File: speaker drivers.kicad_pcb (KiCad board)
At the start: 2 copper layers, 62.9 x 54 mm, 32 parts, among them CN1 68uFE, CN2 10uFE, CN3 0.1uFC

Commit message: Speaker drivers V1 ready for fabrication
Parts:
- removed LOUT1, ROUT1: BNC, LBHB:BNC_Socket_TYCO-AMP_RevA_Date21Jun2010
- added OUT1: CONN_01X04, Socket_Strips:Socket_Strip_Straight_1x04, F.Cu at (88.8, 53.6)
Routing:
- net AGND: track 137.2 -> 118.5 mm
- net Net-(BUFR1-Pad4): track 19.2 -> 29.6 mm, vias 0 -> 1
- net Net-(BUFL1-Pad4): track 19.4 -> 27.0 mm, vias 0 -> 1
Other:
- board size 62.9 x 54 mm -> 54 x 54 mm
- board text added: "LGND"
- board text added: "LOUT"
- board text added: "RGND"
- board text added: "ROUT"

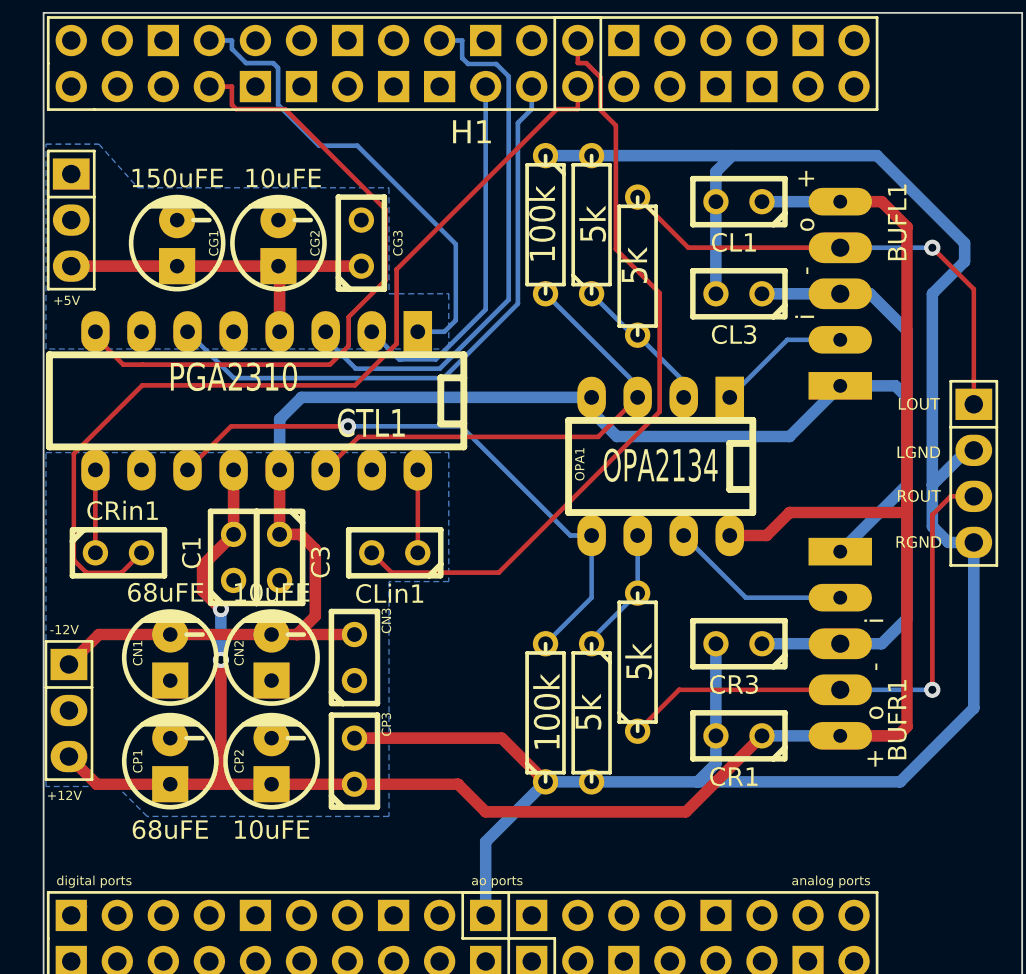
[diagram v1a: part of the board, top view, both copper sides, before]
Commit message: Fixes to speaker driver circuit
* Ensure bypass caps between -12V and GND are correct orientation
* Add notation for all caps indicating size
* Widen drill holes in BUF634
* Ensure cap symbols show orientation when needed
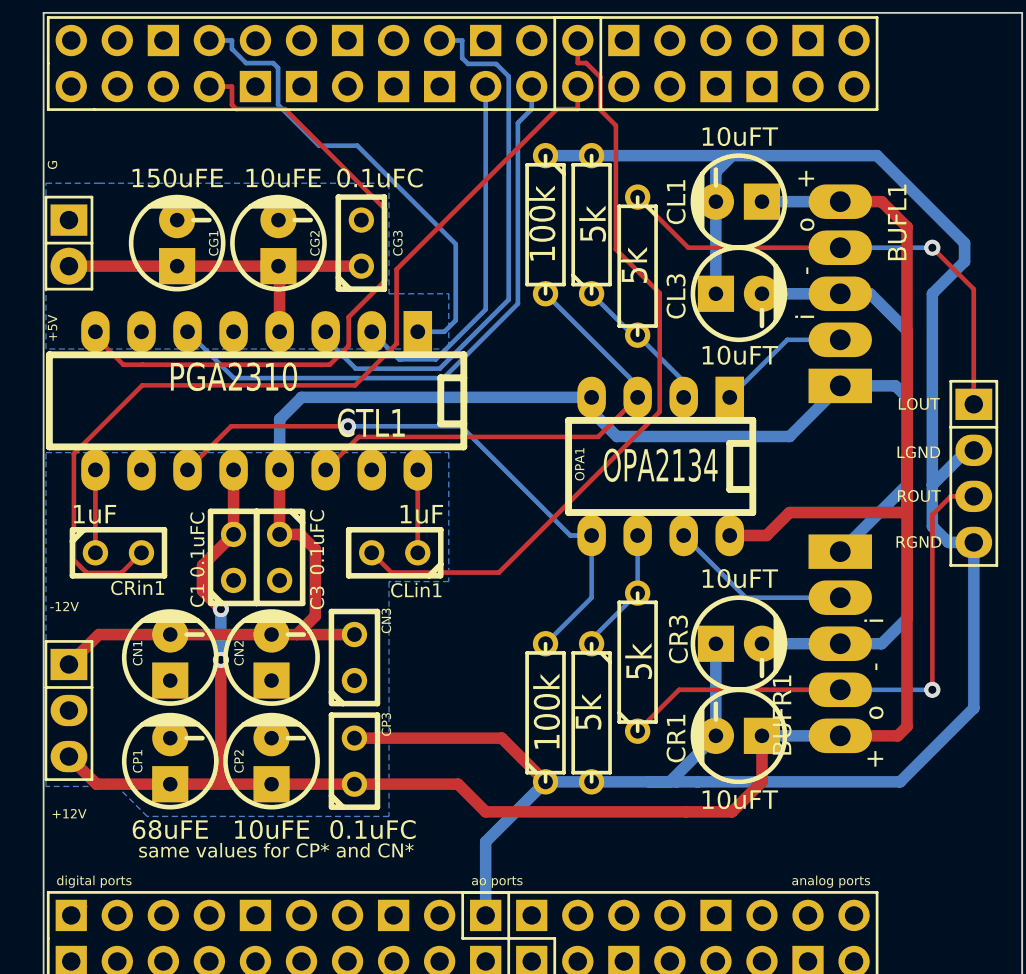
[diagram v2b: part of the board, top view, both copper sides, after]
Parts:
- CL1, CL3, CR1, CR3: footprint Discret:C1 -> Capacitors_ThroughHole:Capacitor5x6RM2.5
- DPWR1: value CONN_01X03 -> CONN_01X02; footprint Socket_Strips:Socket_Strip_Straight_1x03 -> Socket_Strips:Socket_Strip_Straight_1x02
- moved DPWR1 1.28 mm to (38.9, 40.9)
- turned CL1 to 90 degrees
- turned CL3 to 270 degrees
- turned CR1 to 90 degrees
- turned CR3 to 270 degrees
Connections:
- CL3 pad 1: -12V -> AGND
- CL3 pad 2: AGND -> -12V
- CR3 pad 1: -12V -> AGND
- CR3 pad 2: AGND -> -12V
- DPWR1 pad 1: Net-(DPWR1-Pad1) -> DGND
- DPWR1 pad 2: DGND -> +5V
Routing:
- net +12V: track 115.5 -> 117.0 mm
- net AGND: track 118.5 -> 119.9 mm
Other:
- board text added: "G"
- board text added: "same values for CP* and CN*"

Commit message: Commit before modifying speaker driver schematic
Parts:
- removed CG1: 150uFE, Capacitors_ThroughHole:Capacitor5x6RM2.5
- removed CN1, CP1: 68uFE, Capacitors_ThroughHole:Capacitor5x6RM2.5
- removed DPWR1: CONN_01X02, Socket_Strips:Socket_Strip_Straight_1x02
- removed H1: NI_header, LBHB:2x2x18
- removed OUT1: CONN_01X04, Socket_Strips:Socket_Strip_Straight_1x04
- added COMM1: CONN_01X05, Socket_Strips:Socket_Strip_Straight_1x05, F.Cu at (44.5, 36.1)
- added OUTL1: BNC, LBHB:BNC_Socket_TYCO-AMP_RevA_Date21Jun2010, F.Cu at (94.0, 32.0)
- added OUTR1: BNC, LBHB:BNC_Socket_TYCO-AMP_RevA_Date21Jun2010, F.Cu at (94.0, 68.3)
- added SIG1: CONN_01X03, Socket_Strips:Socket_Strip_Straight_1x04, F.Cu at (37.2, 61.1)
- RL1, RL2, RL3, RR1, RR2, RR3: footprint Discret:R3 -> Discret:R5
- moved C1 22.0 mm to (69.9, 56.8), turned to 0 degrees
- moved C3 21.4 mm to (64.8, 42.4), turned to 0 degrees
- moved CLin1 16.7 mm to (41.1, 63.6), turned to 270 degrees
- moved CP3 14.5 mm to (46.6, 57.4), turned to 180 degrees
- moved RL2 14.3 mm to (62.0, 30.5)
- moved CL3 14.3 mm to (74.7, 29.5)
- moved BUFL1 14.2 mm to (81.5, 29.5), turned to 270 degrees
- moved RL3 11.9 mm to (57.9, 30.5)
- moved RL1 9.54 mm to (66.0, 30.5)
- moved APWR1 9.28 mm to (48.1, 67.1), turned to 0 degrees
- moved RR2 9.09 mm to (62.0, 67.8)
- moved CG3 9.02 mm to (46.0, 40.6), turned to 270 degrees
- moved CP2 8.70 mm to (46.6, 61.5), turned to 90 degrees
- moved CG2 8.51 mm to (41.9, 40.6), turned to 180 degrees
- moved RR3 7.36 mm to (57.8, 67.8)
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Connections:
- CTL1 pad 1: /ZCEN -> DGND
- CTL1 pad 10: AGND -> Net-(CTL1-Pad10)
- CTL1 pad 15: AGND -> Net-(CTL1-Pad10)
- CTL1 pad 7: Net-(CTL1-Pad7) -> (no net)
- CTL1 pad 8: /MUTE -> +5V
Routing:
- net +12V: track 117.0 -> 50.1 mm, vias 2 -> 0
- net -12V: track 108.1 -> 43.1 mm
- net AGND: track 119.9 -> 57.0 mm
- net Net-(CRin1-Pad2): track 49.7 -> 4.99 mm
- net Net-(CLin1-Pad2): track 42.6 -> 4.99 mm
- net /MUTE: track 36.8 -> 0.00 mm
- net Net-(CTL1-Pad11): track 32.8 -> 0.00 mm, vias 1 -> 0
- net Net-(CTL1-Pad14): track 26.7 -> 0.00 mm
- net /ZCEN: track 26.3 -> 0.00 mm
- net Net-(BUFR1-Pad4): track 29.6 -> 7.44 mm, vias 1 -> 0
- net /SCLK: track 33.3 -> 13.7 mm
- net Net-(BUFL1-Pad4): track 27.0 -> 7.44 mm, vias 1 -> 0
- net /SDI: track 30.3 -> 12.2 mm
- net +5V: track 19.8 -> 31.7 mm
- net Net-(BUFR1-Pad2): track 10.1 -> 0.00 mm
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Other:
- net class High current signal added: clearance 0.508, trace_width 0.635, via_dia 0.889, via_drill 0.635
- board text removed: "+12V"
- board text removed: "+5V"
- board text removed: "-12V"
- board text removed: "G"
- board text removed: "LGND"
- board text removed: "LOUT"
- board text removed: "RGND"
- board text removed: "ROUT"
- board text removed: "same values for CP* and CN*"

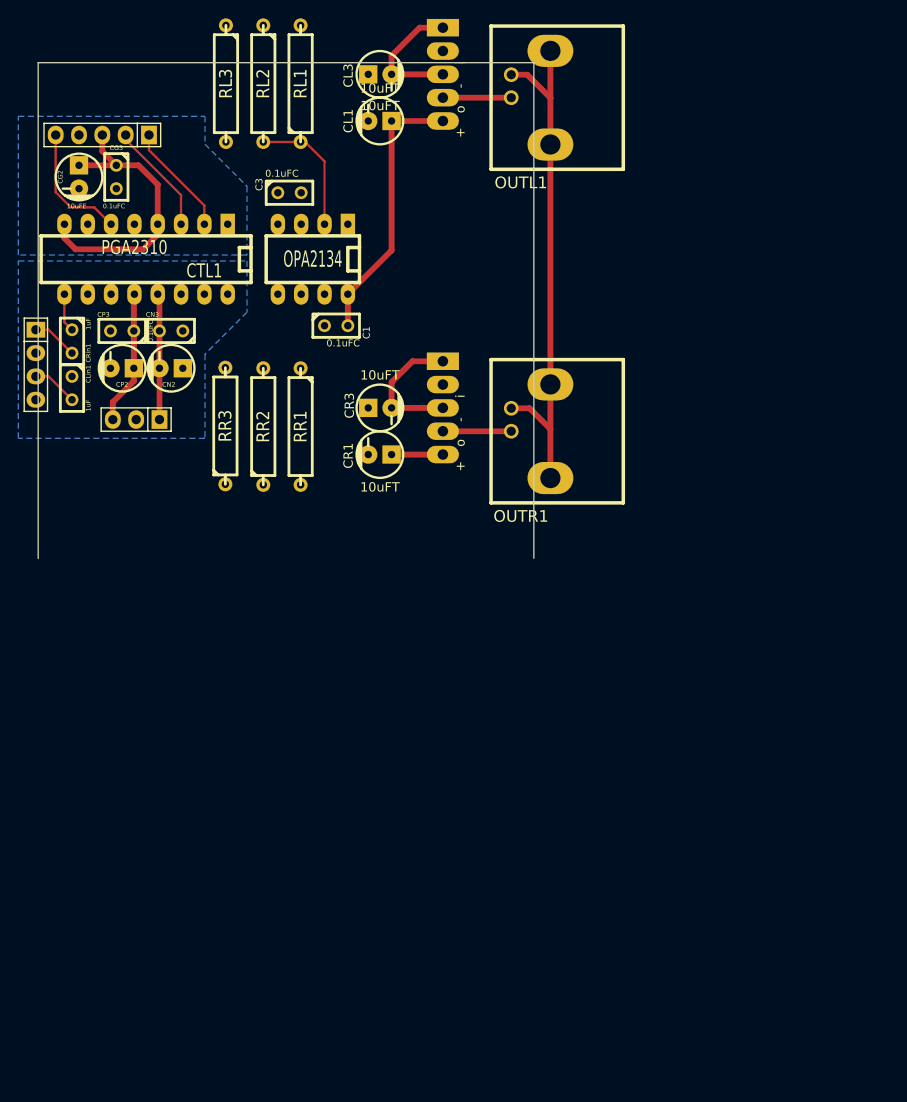
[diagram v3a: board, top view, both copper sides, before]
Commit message: ENH: Working draft of speaker drivers v2
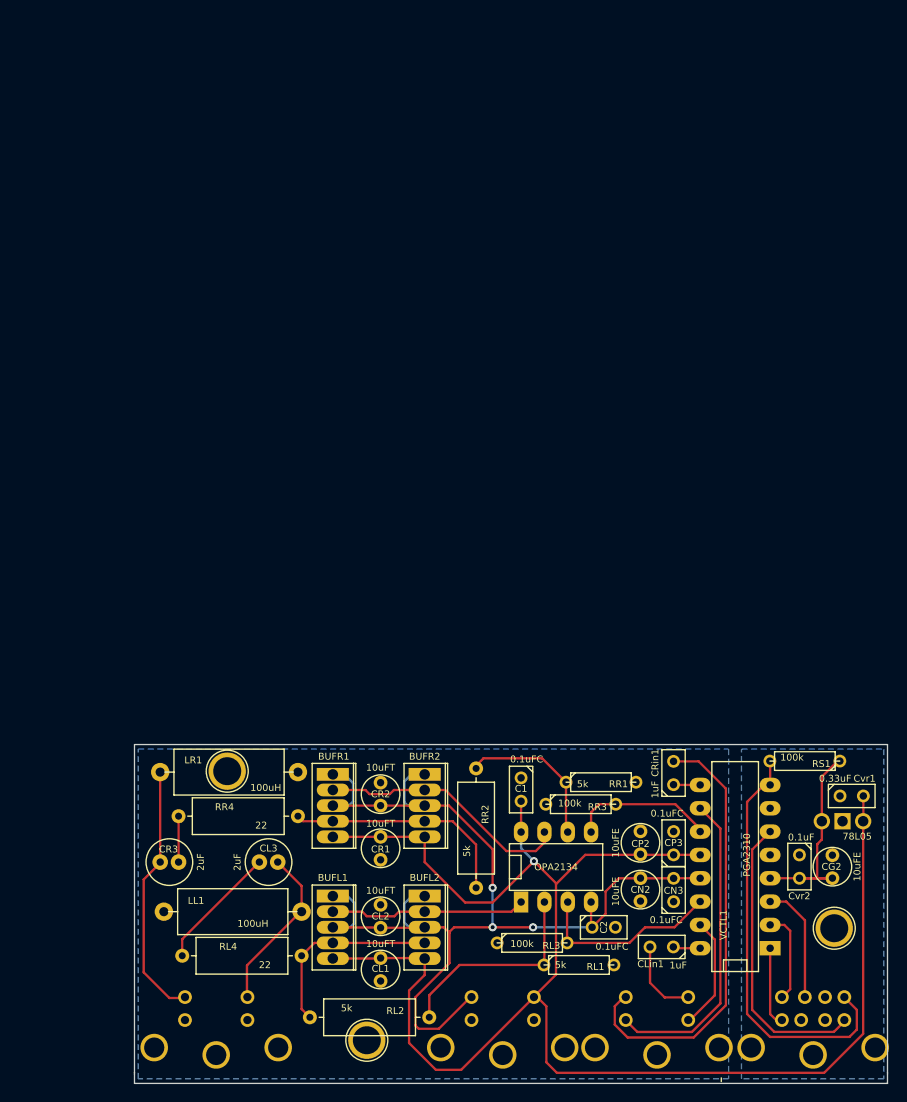
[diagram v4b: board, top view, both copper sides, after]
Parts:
- removed APWR1: CONN_01X03, Socket_Strips:Socket_Strip_Straight_1x03
- removed C3, CG3: 0.1uFC, Discret:C1
- removed COMM1: CONN_01X05, Socket_Strips:Socket_Strip_Straight_1x05
- removed CTL1: PGA2310, Sockets_DIP:DIP-16__300_ELL
- removed OUTL1, OUTR1: BNC, LBHB:BNC_Socket_TYCO-AMP_RevA_Date21Jun2010
- removed SIG1: CONN_01X03, Socket_Strips:Socket_Strip_Straight_1x04
- added 1pin: VAL**, Connect:1pin, F.Cu at (73.2, 134.6)
- added 1pin: VAL**, Connect:1pin, F.Cu at (58.0, 105.3)
- added 1pin: VAL**, Connect:1pin, F.Cu at (124.2, 122.4)
- added BUFL2: BUF634, LBHB:BUF634, F.Cu at (79.5, 122.3)
- added BUFR2: BUF634, LBHB:BUF634, F.Cu at (79.5, 109.1)
- added C2: 0.1uFC, LBHB:C1, F.Cu at (99.0, 122.3)
- added CL2: 10uFT, LBHB:Capacitor4D2.4L, F.Cu at (74.8, 121.1)
- added CR2: 10uFT, LBHB:Capacitor4D2.4L, F.Cu at (74.8, 107.8)
- added Cvr1: 0.33uF, LBHB:C1, F.Cu at (126.0, 108.0)
- added Cvr2: 0.1uF, LBHB:C1, F.Cu at (120.4, 115.7)
- added LL1: 100uH, LBHB:inductor-12mm, F.Cu at (58.6, 122.6)
- added LR1: 100uH, LBHB:inductor-12mm, F.Cu at (58.2, 103.4)
- added PWR1: 4P_miniDIN_PWR, LBHB:4P-mini-DIN-grounded, F.Cu at (88.0, 140.9)
- added RL4: 22, LBHB:13x4mm-resistor, F.Cu at (59.6, 125.4)
- added RR4: 22, LBHB:13x4mm-resistor, F.Cu at (59.2, 110.2)
- added RS1: 100k, Discret:R3, F.Cu at (121.0, 104.2)
- added SER1: 8P_miniDIN, LBHB:8P-mini-DIN-grounded, F.Cu at (121.8, 140.9)
- added SIGIN1: 4P_miniDIN, LBHB:4P-mini-DIN, F.Cu at (104.8, 140.9)
- added SIGOUT1: 4P_miniDIN, LBHB:4P-mini-DIN-grounded, F.Cu at (56.9, 140.9)
- added VCTL1: PGA2310, Sockets_DIP:DIP-16__300_ELL, F.Cu at (113.4, 115.7)
- added VREG1: 78L05, LBHB:78LXX, F.Cu at (125.0, 110.8)
- C1, CLin1, CN3, CP3, CRin1: footprint Discret:C1 -> LBHB:C1
- CG2, CL1, CN2, CP2, CR1: footprint Capacitors_ThroughHole:Capacitor5x6RM2.5 -> LBHB:Capacitor4D2.4L
- CL3, CR3: value 10uFT -> 2uF; footprint Capacitors_ThroughHole:Capacitor5x6RM2.5 -> LBHB:Capacitor5x11MuseES
- OPA1: footprint Sockets_DIP:DIP-8__300_ELL -> LBHB:DIP-8__300_ELL
- RL1, RL3, RR1, RR3: footprint Discret:R5 -> Discret:R3
- RL2, RR2: footprint Discret:R5 -> LBHB:13x4mm-resistor
- moved CG2 111.2 mm to (124.0, 115.7), turned to 90 degrees
- moved RL2 102.3 mm to (73.5, 132.1), turned to 0 degrees
- moved RL1 100.6 mm to (96.3, 126.4), turned to 0 degrees
- moved RL3 99.3 mm to (91.2, 124.0), turned to 0 degrees
- moved BUFL1 93.6 mm to (69.5, 122.3)
- moved CL1 92.4 mm to (74.8, 126.9), turned to 270 degrees
- moved CLin1 88.5 mm to (105.4, 124.5), turned to 180 degrees
- moved CL3 86.6 mm to (62.5, 115.2)
- moved CP3 82.0 mm to (106.7, 113.2), turned to 90 degrees
- moved CN3 81.9 mm to (106.7, 118.3), turned to 90 degrees
- moved CRin1 80.6 mm to (106.7, 105.5), turned to 90 degrees
- moved CP2 76.5 mm to (103.0, 113.1)
- moved CN2 76.4 mm to (103.0, 118.2)
- moved OPA1 71.3 mm to (93.9, 115.8), turned to 0 degrees
- moved RR3 56.5 mm to (96.5, 108.9), turned to 0 degrees
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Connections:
- CG2 pad 1: +5V -> Net-(CG2-Pad1)
- CL3 pad 1: AGND -> Net-(CL3-Pad1)
- CL3 pad 2: -12V -> Net-(CL3-Pad2)
- CR3 pad 1: AGND -> Net-(CR3-Pad1)
- CR3 pad 2: -12V -> Net-(CR3-Pad2)
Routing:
- net +12V: track 50.1 -> 179.0 mm, vias 0 -> 1
- net -12V: track 43.1 -> 124.6 mm, vias 0 -> 3
- net AGND: track 57.0 -> 0.00 mm
- net /MUTE: track 0.00 -> 46.6 mm
- net Net-(CRin1-Pad2): track 4.99 -> 48.3 mm
- net Net-(SIGIN1-Pad2): track 0.00 -> 34.3 mm
- net +5V: track 31.7 -> 0.00 mm
- net Net-(CR3-Pad2): track 0.00 -> 28.2 mm
- net Net-(BUFR1-Pad2): track 0.00 -> 27.7 mm
- net Net-(CG2-Pad1): track 0.00 -> 24.8 mm
- net Net-(BUFL1-Pad2): track 0.00 -> 21.3 mm
- net Net-(OPA1-Pad3): track 0.00 -> 20.8 mm
- net Net-(CL3-Pad2): track 0.00 -> 18.4 mm
- net /SCLK: track 13.7 -> 31.8 mm
- net Net-(BUFR1-Pad4): track 7.44 -> 25.5 mm
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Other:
- board size 54 x 54 mm -> 82 x 36.9 mm
- net class High current signal: clearance 0.508 -> 0.254; trace_width 0.635 -> 0.254
- net class Power: clearance 0.508 -> 0.254; trace_width 0.635 -> 0.254
- board text added: "Speaker Driver V2 Design by BNB (OHSU LBHB) bburan@alum.mit.edu 2015.02.13"
- board text removed: "Speaker Driver V1 Design by BNB (OHSU LBHB) bburan@alum.mit.edu 2014.09.17"
